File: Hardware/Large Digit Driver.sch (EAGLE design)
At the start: 28 parts, among them U1 TPIC6C596

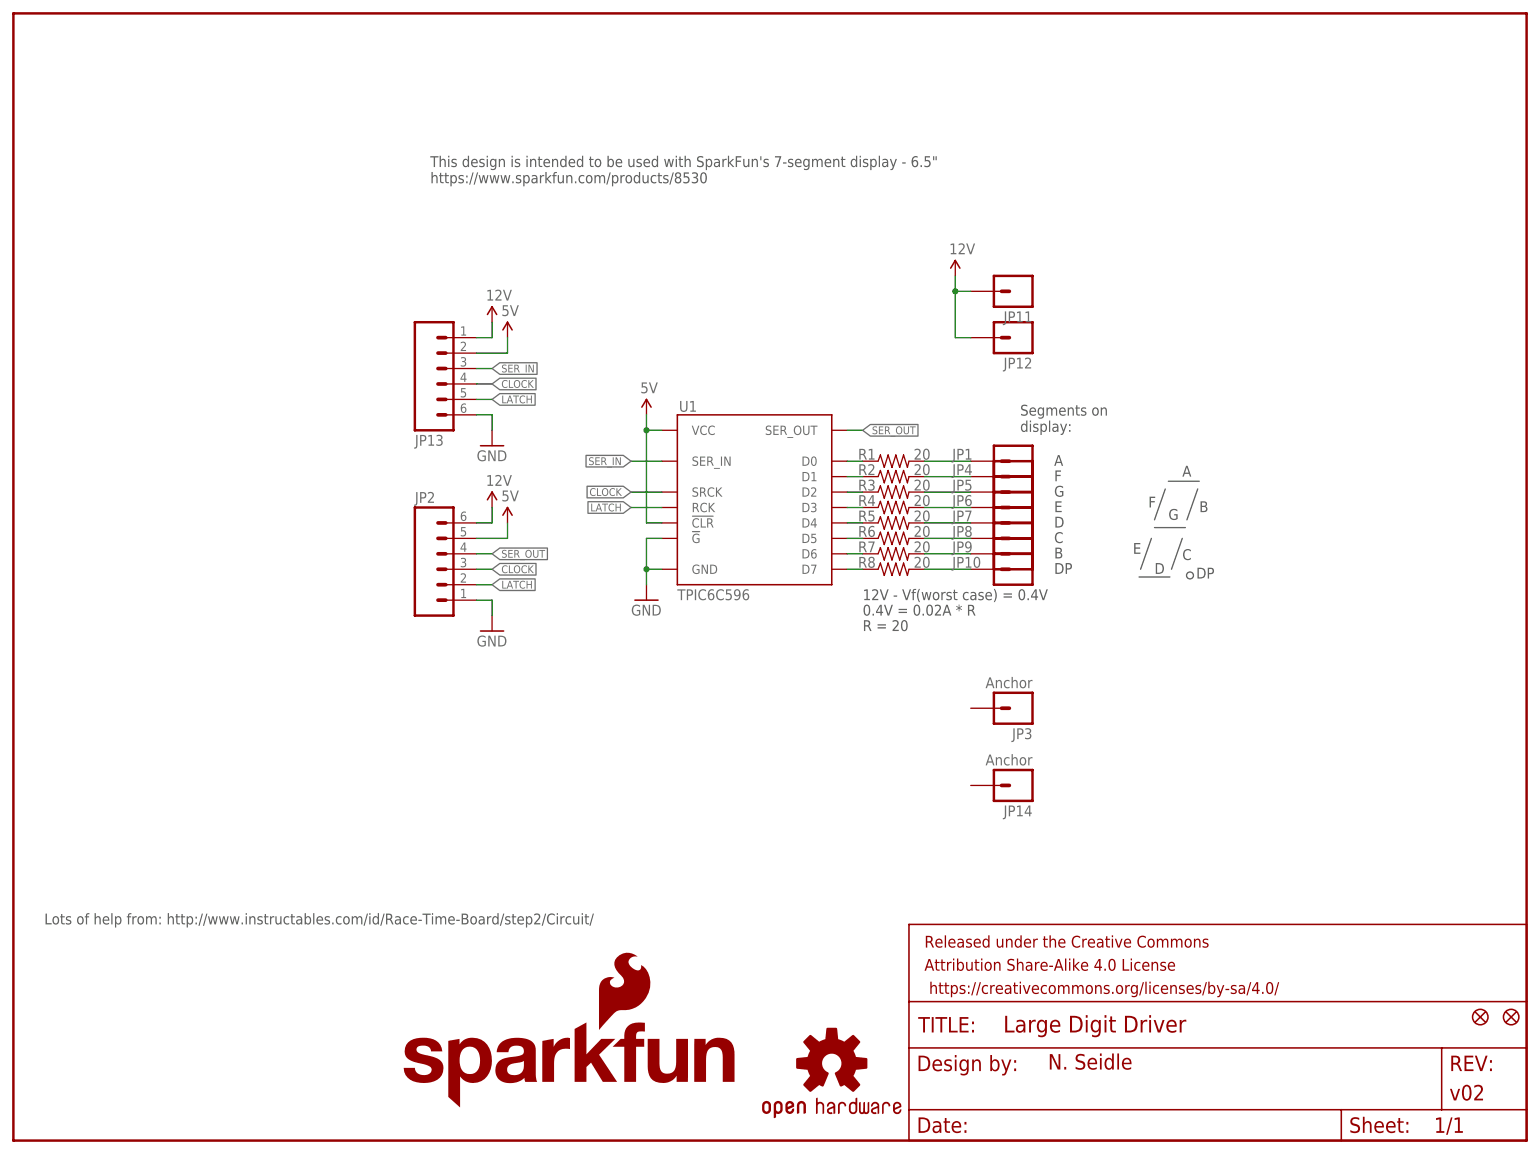
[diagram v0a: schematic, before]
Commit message: Changing to 15 Ohm limiting resistors. Adding example code.
20 Ohm resistors brought current down to 11mA in testing. Decreasing
resistor size to get higher current per segment.
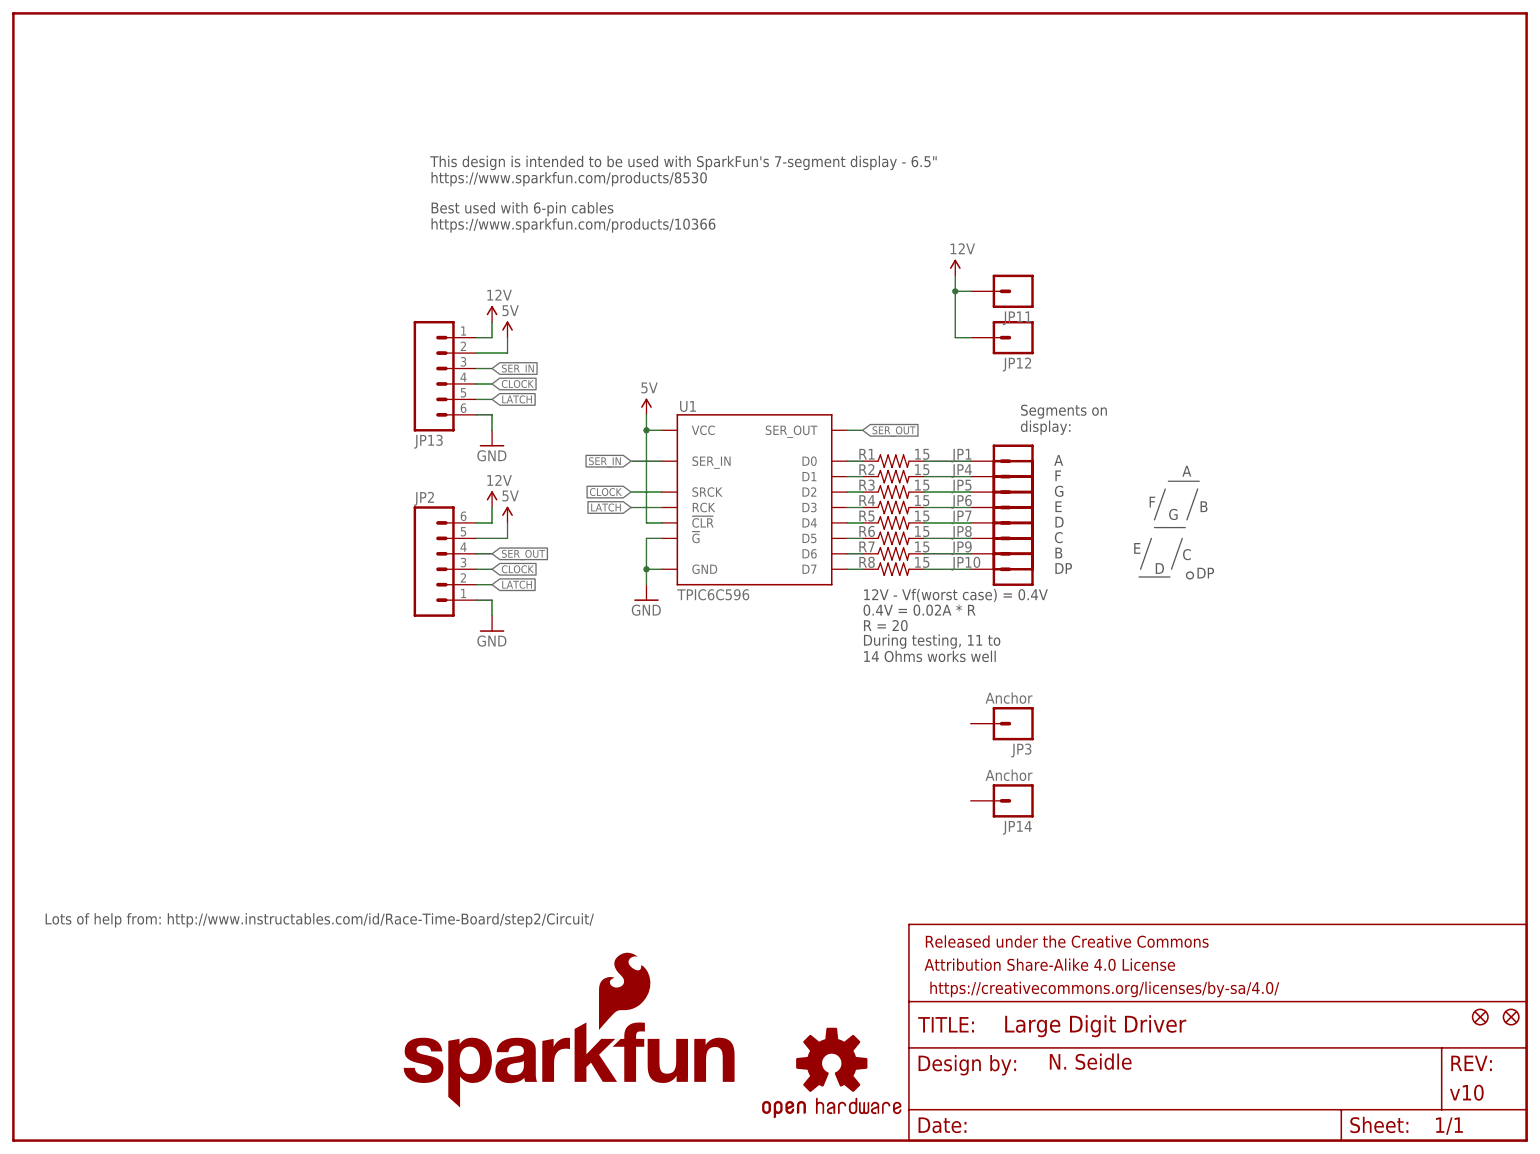
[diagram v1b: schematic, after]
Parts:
- FRAME1: VERSION v02 -> v10
- R1, R2, R3, R4, R5, R6, R7, R8: value 20 -> 15; device SparkFun-Resistors:20OHM1/10W1%(0603)SMD -> SparkFun-Resistors:15OHM-1/10W-1%(0603)0603
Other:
- note added: "Best used with 6-pin cables https://www.sparkfun.com/products/10366"
- note added: "During testing, 11 to 14 Ohms works well"
- moved on the sheet: JP14, JP3
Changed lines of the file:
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@@
 <?xml version="1.0" encoding="utf-8"?>
 <!DOCTYPE eagle SYSTEM "eagle.dtd">
-<eagle version="7.2.0">
+<eagle version="7.1.0">
 <drawing>
 <settings>
@@
 <part name="FRAME1" library="SparkFun-Aesthetics" deviceset="FRAME-LETTER" device="">
 <attribute name="DESIGNER" value="N. Seidle"/>
-<attribute name="VERSION" value="v02"/>
+<attribute name="VERSION" value="v10"/>
 </part>
 <part name="SUPPLY1" library="SparkFun-Aesthetics" deviceset="5V" device=""/>
@@
 <part name="SUPPLY5" library="SparkFun-Aesthetics" deviceset="12V" device=""/>
 <part name="LOGO1" library="SparkFun-Aesthetics" deviceset="SFE_LOGO_NAME_FLAME" device=".1_INCH"/>
-<part name="R1" library="SparkFun-Resistors" deviceset="20OHM1/10W1%(0603)" device="SMD" value="20"/>
-<part name="R2" library="SparkFun-Resistors" deviceset="20OHM1/10W1%(0603)" device="SMD" value="20"/>
-<part name="R3" library="SparkFun-Resistors" deviceset="20OHM1/10W1%(0603)" device="SMD" value="20"/>
-<part name="R4" library="SparkFun-Resistors" deviceset="20OHM1/10W1%(0603)" device="SMD" value="20"/>
-<part name="R5" library="SparkFun-Resistors" deviceset="20OHM1/10W1%(0603)" device="SMD" value="20"/>
-<part name="R6" library="SparkFun-Resistors" deviceset="20OHM1/10W1%(0603)" device="SMD" value="20"/>
-<part name="R7" library="SparkFun-Resistors" deviceset="20OHM1/10W1%(0603)" device="SMD" value="20"/>
-<part name="R8" library="SparkFun-Resistors" deviceset="20OHM1/10W1%(0603)" device="SMD" value="20"/>
+<part name="R1" library="SparkFun-Resistors" deviceset="15OHM-1/10W-1%(0603)" device="0603" value="15"/>
+<part name="R2" library="SparkFun-Resistors" deviceset="15OHM-1/10W-1%(0603)" device="0603" value="15"/>
+<part name="R3" library="SparkFun-Resistors" deviceset="15OHM-1/10W-1%(0603)" device="0603" value="15"/>
+<part name="R4" library="SparkFun-Resistors" deviceset="15OHM-1/10W-1%(0603)" device="0603" value="15"/>
+<part name="R5" library="SparkFun-Resistors" deviceset="15OHM-1/10W-1%(0603)" device="0603" value="15"/>
+<part name="R6" library="SparkFun-Resistors" deviceset="15OHM-1/10W-1%(0603)" device="0603" value="15"/>
+<part name="R7" library="SparkFun-Resistors" deviceset="15OHM-1/10W-1%(0603)" device="0603" value="15"/>
+<part name="R8" library="SparkFun-Resistors" deviceset="15OHM-1/10W-1%(0603)" device="0603" value="15"/>
 <part name="JP13" library="SparkFun-Connectors" deviceset="M06" device="SMD"/>
 <part name="U1" library="SparkFun-DigitalIC" deviceset="TPIC6C596" device="SOIC" value="TPIC6C596"/>
@@
 <text x="68.58" y="157.48" size="1.778" layer="97">This design is intended to be used with SparkFun's 7-segment display - 6.5"
 https://www.sparkfun.com/products/8530</text>
+<text x="139.7" y="78.74" size="1.778" layer="97">During testing, 11 to
+14 Ohms works well</text>
+<text x="68.58" y="149.86" size="1.778" layer="97">Best used with 6-pin cables
+https://www.sparkfun.com/products/10366</text>
 </plain>
 <instances>
@@
 <instance part="JP13" gate="G$1" x="71.12" y="127" rot="MR180"/>
 <instance part="U1" gate="U1" x="121.92" y="106.68"/>
-<instance part="JP3" gate="G$1" x="165.1" y="71.12" rot="R180"/>
-<instance part="JP14" gate="G$1" x="165.1" y="58.42" rot="R180"/>
+<instance part="JP3" gate="G$1" x="165.1" y="68.58" rot="R180"/>
+<instance part="JP14" gate="G$1" x="165.1" y="55.88" rot="R180"/>
 <instance part="FID1" gate="G$1" x="246.38" y="20.32"/>
 <instance part="FID2" gate="G$1" x="241.3" y="20.32"/>

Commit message: Added silk to anchors. Added power notes to schematic.
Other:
- note added: "Board reqiures both 12V for the LEDs and 5V for the IC."
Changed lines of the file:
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@@
 <?xml version="1.0" encoding="utf-8"?>
 <!DOCTYPE eagle SYSTEM "eagle.dtd">
-<eagle version="7.1.0">
+<eagle version="7.2.0">
 <drawing>
 <settings>
@@
 <text x="139.7" y="86.36" size="1.778" layer="97">0.4V = 0.02A * R</text>
 <text x="139.7" y="83.82" size="1.778" layer="97">R = 20</text>
-<text x="68.58" y="157.48" size="1.778" layer="97">This design is intended to be used with SparkFun's 7-segment display - 6.5"
+<text x="68.58" y="165.1" size="1.778" layer="97">This design is intended to be used with SparkFun's 7-segment display - 6.5"
 https://www.sparkfun.com/products/8530</text>
 <text x="139.7" y="78.74" size="1.778" layer="97">During testing, 11 to
 14 Ohms works well</text>
-<text x="68.58" y="149.86" size="1.778" layer="97">Best used with 6-pin cables
+<text x="68.58" y="157.48" size="1.778" layer="97">Best used with 6-pin cables
 https://www.sparkfun.com/products/10366</text>
+<text x="68.58" y="149.86" size="1.778" layer="97">Board reqiures both 12V for
+the LEDs and 5V for the IC.</text>
 </plain>
 <instances>
